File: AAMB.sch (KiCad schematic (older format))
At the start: 13 parts, among them J1 Screw_Terminal_01x04, J2 PJRAS4X2U01X, J3 SPKR, J4 SPKR, J5 Screw_Terminal_01x03, J6 Screw_Terminal_01x03, J7 Screw_Terminal_01x04

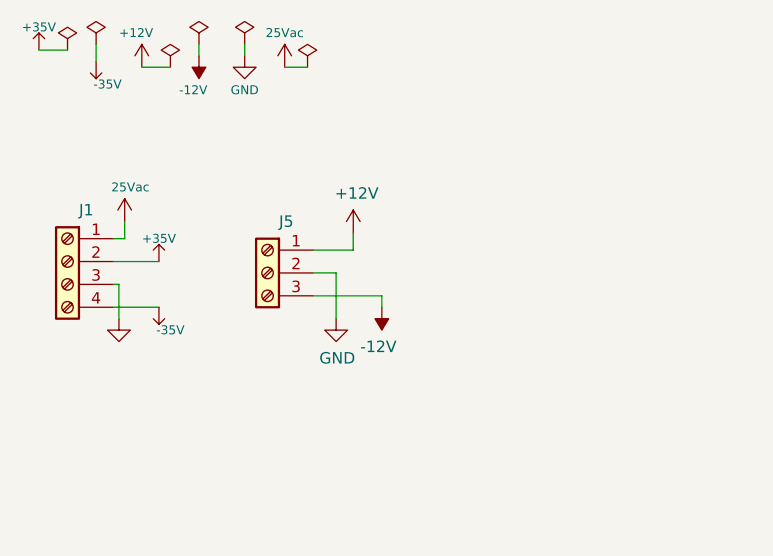
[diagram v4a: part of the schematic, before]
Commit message: Layout startover, sorting, some routing. Removed redundant fuses. BOM export.
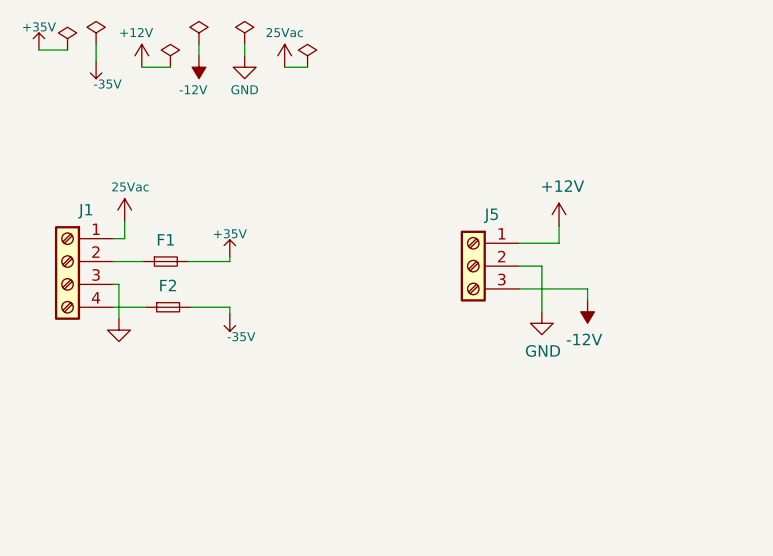
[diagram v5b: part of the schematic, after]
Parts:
- added F1, F2: Fuse_Small, Resistor_SMD:R_1206_3216Metric_Pad1.42x1.75mm_HandSolder, symbol Device:Fuse_Small
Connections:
- net +35V: now also F1.2; no longer J1.2 (Pin_2)
- net -35V: now also F2.2; no longer J1.4 (Pin_4)
- new net: F1.1, J1.2 (Pin_2)
- new net: F2.1, J1.4 (Pin_4)
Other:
- moved on the sheet: J5
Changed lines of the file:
@@
 L AAMB-rescue:+35V-Power-amp #PWR0106
 U 1 1 5E1EC4AA
-P 1100 1550
-F 0 "#PWR0106" H 1275 1375 50  0001 C CNN
-F 1 "+35V" H 1100 1650 39  0000 C CNN
-F 2 "" H 1100 1550 50  0001 C CNN
-F 3 "" H 1100 1550 50  0001 C CNN
-	1    1100 1550
+P 1410 1530
+F 0 "#PWR0106" H 1585 1355 50  0001 C CNN
+F 1 "+35V" H 1410 1630 39  0000 C CNN
+F 2 "" H 1410 1530 50  0001 C CNN
+F 3 "" H 1410 1530 50  0001 C CNN
+	1    1410 1530
 	1    0    0    -1
 $EndComp
@@
 L AAMB-rescue:-35V-Power-amp #PWR0107
 U 1 1 5E1EDDCB
-P 1100 1750
-F 0 "#PWR0107" H 1275 1575 50  0001 C CNN
-F 1 "-35V" H 1150 1650 39  0000 C CNN
-F 2 "" H 1100 1750 50  0001 C CNN
-F 3 "" H 1100 1750 50  0001 C CNN
-	1    1100 1750
-	1    0    0    -1
-$EndComp
-Wire Wire Line
-	900  1750 1100 1750
-Wire Wire Line
-	900  1550 1100 1550
+P 1410 1780
+F 0 "#PWR0107" H 1585 1605 50  0001 C CNN
+F 1 "-35V" H 1460 1680 39  0000 C CNN
+F 2 "" H 1410 1780 50  0001 C CNN
+F 3 "" H 1410 1780 50  0001 C CNN
+	1    1410 1780
+	1    0    0    -1
+$EndComp
 $Comp
 L power:PWR_FLAG #FLG0101
@@
 L Connector:Screw_Terminal_01x03 J5
 U 1 1 5E426C78
-P 1575 1600
-F 0 "J5" H 1493 1825 50  0000 C CNN
-F 1 "Screw_Terminal_01x03" H 1493 1826 50  0001 C CNN
-F 2 "TerminalBlock_Phoenix:TerminalBlock_Phoenix_MKDS-1,5-3_1x03_P5.00mm_Horizontal" H 1575 1600 50  0001 C CNN
-F 3 "https://media.digikey.com/pdf/Data%20Sheets/Phoenix%20Contact%20PDFs/1935174.pdf" H 1575 1600 50  0001 C CNN
-F 4 "https://www.digikey.com/product-detail/en/phoenix-contact/1935174/277-1578-ND/568615" H 1575 1600 50  0001 C CNN "DigiKey"
-F 5 "Phoenix Contact" H 1575 1600 50  0001 C CNN "MFG"
-F 6 "1935174" H 1575 1600 50  0001 C CNN "MPN"
-	1    1575 1600
+P 2475 1570
+F 0 "J5" H 2393 1795 50  0000 C CNN
+F 1 "Screw_Terminal_01x03" H 2393 1796 50  0001 C CNN
+F 2 "TerminalBlock_Phoenix:TerminalBlock_Phoenix_MKDS-1,5-3_1x03_P5.00mm_Horizontal" H 2475 1570 50  0001 C CNN
+F 3 "https://media.digikey.com/pdf/Data%20Sheets/Phoenix%20Contact%20PDFs/1935174.pdf" H 2475 1570 50  0001 C CNN
+F 4 "https://www.digikey.com/product-detail/en/phoenix-contact/1935174/277-1578-ND/568615" H 2475 1570 50  0001 C CNN "DigiKey"
+F 5 "Phoenix Contact" H 2475 1570 50  0001 C CNN "MFG"
+F 6 "1935174" H 2475 1570 50  0001 C CNN "MPN"
+	1    2475 1570
 	-1   0    0    -1
 $EndComp
@@
 L power:+12V #PWR09
 U 1 1 5E4290D4
-P 1950 1425
-F 0 "#PWR09" H 1950 1275 50  0001 C CNN
-F 1 "+12V" H 1965 1598 50  0000 C CNN
-F 2 "" H 1950 1425 50  0001 C CNN
-F 3 "" H 1950 1425 50  0001 C CNN
-	1    1950 1425
+P 2850 1395
+F 0 "#PWR09" H 2850 1245 50  0001 C CNN
+F 1 "+12V" H 2865 1568 50  0000 C CNN
+F 2 "" H 2850 1395 50  0001 C CNN
+F 3 "" H 2850 1395 50  0001 C CNN
+	1    2850 1395
 	1    0    0    -1
 $EndComp
@@
 L power:-12V #PWR010
 U 1 1 5E429F52
-P 2075 1750
-F 0 "#PWR010" H 2075 1850 50  0001 C CNN
-F 1 "-12V" H 2090 1923 50  0000 C CNN
-F 2 "" H 2075 1750 50  0001 C CNN
-F 3 "" H 2075 1750 50  0001 C CNN
-	1    2075 1750
+P 2975 1720
+F 0 "#PWR010" H 2975 1820 50  0001 C CNN
+F 1 "-12V" H 2990 1893 50  0000 C CNN
+F 2 "" H 2975 1720 50  0001 C CNN
+F 3 "" H 2975 1720 50  0001 C CNN
+	1    2975 1720
 	-1   0    0    1
 $EndComp
@@
 L power:GND #PWR08
 U 1 1 5E42A7CB
-P 1875 1800
-F 0 "#PWR08" H 1875 1550 50  0001 C CNN
-F 1 "GND" H 1880 1627 50  0000 C CNN
-F 2 "" H 1875 1800 50  0001 C CNN
-F 3 "" H 1875 1800 50  0001 C CNN
-	1    1875 1800
-	1    0    0    -1
-$EndComp
-Wire Wire Line
-	1875 1800 1875 1600
-Wire Wire Line
-	1875 1600 1775 1600
-Wire Wire Line
-	1950 1425 1950 1500
-Wire Wire Line
-	1950 1500 1775 1500
-Wire Wire Line
-	2075 1700 1775 1700
-Wire Wire Line
-	2075 1750 2075 1700
+P 2775 1770
+F 0 "#PWR08" H 2775 1520 50  0001 C CNN
+F 1 "GND" H 2780 1597 50  0000 C CNN
+F 2 "" H 2775 1770 50  0001 C CNN
+F 3 "" H 2775 1770 50  0001 C CNN
+	1    2775 1770
+	1    0    0    -1
+$EndComp
+Wire Wire Line
+	2775 1770 2775 1570
+Wire Wire Line
+	2775 1570 2675 1570
+Wire Wire Line
+	2850 1395 2850 1470
+Wire Wire Line
+	2850 1470 2675 1470
+Wire Wire Line
+	2975 1670 2675 1670
+Wire Wire Line
+	2975 1720 2975 1670
 Text Label 6725 4175 2    50   ~ 0
 line_audio_R
@@
 F 1 "TP" H 4950 5129 50  0000 C CNN
 F 2 "TestPoint:TestPoint_2Pads_Pitch2.54mm_Drill0.8mm" H 4950 5025 50  0001 C CNN
-F 3 "~" H 4950 5025 50  0001 C CNN
+F 3 "" H 4950 5025 50  0001 C CNN
 	1    4950 5025
 	1    0    0    -1
@@
 F 1 "TP" H 4950 5554 50  0001 C CNN
 F 2 "TestPoint:TestPoint_2Pads_Pitch2.54mm_Drill0.8mm" H 4950 5450 50  0001 C CNN
-F 3 "~" H 4950 5450 50  0001 C CNN
+F 3 "" H 4950 5450 50  0001 C CNN
 F 4 "pre_vol_audio_R" H 4945 5365 50  0000 C CNN "Note"
 	1    4950 5450
@@
 F 1 "TP" H 6700 4729 50  0000 C CNN
 F 2 "TestPoint:TestPoint_2Pads_Pitch2.54mm_Drill0.8mm" H 6700 4625 50  0001 C CNN
-F 3 "~" H 6700 4625 50  0001 C CNN
+F 3 "" H 6700 4625 50  0001 C CNN
 	1    6700 4625
 	1    0    0    -1
@@
 F 1 "TP" H 6700 5154 50  0000 C CNN
 F 2 "TestPoint:TestPoint_2Pads_Pitch2.54mm_Drill0.8mm" H 6700 5050 50  0001 C CNN
-F 3 "~" H 6700 5050 50  0001 C CNN
+F 3 "" H 6700 5050 50  0001 C CNN
 	1    6700 5050
 	1    0    0    -1
@@
 F 1 "TP" H 8350 4829 50  0000 C CNN
 F 2 "TestPoint:TestPoint_2Pads_Pitch2.54mm_Drill0.8mm" H 8350 4725 50  0001 C CNN
-F 3 "~" H 8350 4725 50  0001 C CNN
+F 3 "" H 8350 4725 50  0001 C CNN
 	1    8350 4725
 	1    0    0    -1
@@
 F 1 "TP" H 8350 5254 50  0000 C CNN
 F 2 "TestPoint:TestPoint_2Pads_Pitch2.54mm_Drill0.8mm" H 8350 5150 50  0001 C CNN
-F 3 "~" H 8350 5150 50  0001 C CNN
+F 3 "" H 8350 5150 50  0001 C CNN
 	1    8350 5150
 	1    0    0    -1
@@
 	1    0    0    -1
 $EndComp
+$Comp
+L Device:Fuse_Small F?
+U 1 1 5E9A4ADA
+P 1130 1550
+AR Path="/5C7F608F/5E9A4ADA" Ref="F?"  Part="1"
+AR Path="/5E9A4ADA" Ref="F1"  Part="1"
+F 0 "F1" H 1130 1643 50  0000 C CNN
+F 1 "Fuse_Small" H 1130 1644 50  0001 C CNN
+F 2 "Resistor_SMD:R_1206_3216Metric_Pad1.42x1.75mm_HandSolder" H 1130 1550 50  0001 C CNN
+F 3 "https://belfuse.com/resources/datasheets/circuitprotection/ds-cp-c1f-series.pdf" H 1130 1550 50  0001 C CNN
+F 4 "https://www.digikey.com/product-detail/en/bel-fuse-inc/C1F-3/507-1883-1-ND/4968162" H 1130 1550 50  0001 C CNN "DigiKey"
+F 5 "Bel Fuse Inc." H 1130 1550 50  0001 C CNN "MFG"
+F 6 "C1F 3" H 1130 1550 50  0001 C CNN "MPN"
+	1    1130 1550
+	1    0    0    -1
+$EndComp
+Wire Wire Line
+	900  1550 1030 1550
+Wire Wire Line
+	1230 1550 1410 1550
+Wire Wire Line
+	1410 1550 1410 1530
+$Comp
+L Device:Fuse_Small F?
+U 1 1 5E9B7B14
+P 1140 1750
+AR Path="/5C7F608F/5E9B7B14" Ref="F?"  Part="1"
+AR Path="/5E9B7B14" Ref="F2"  Part="1"
+F 0 "F2" H 1140 1843 50  0000 C CNN
+F 1 "Fuse_Small" H 1140 1844 50  0001 C CNN
+F 2 "Resistor_SMD:R_1206_3216Metric_Pad1.42x1.75mm_HandSolder" H 1140 1750 50  0001 C CNN
+F 3 "https://belfuse.com/resources/datasheets/circuitprotection/ds-cp-c1f-series.pdf" H 1140 1750 50  0001 C CNN
+F 4 "https://www.digikey.com/product-detail/en/bel-fuse-inc/C1F-3/507-1883-1-ND/4968162" H 1140 1750 50  0001 C CNN "DigiKey"
+F 5 "Bel Fuse Inc." H 1140 1750 50  0001 C CNN "MFG"
+F 6 "C1F 3" H 1140 1750 50  0001 C CNN "MPN"
+	1    1140 1750
+	1    0    0    -1
+$EndComp
+Wire Wire Line
+	900  1750 1040 1750
+Wire Wire Line
+	1240 1750 1410 1750
+Wire Wire Line
+	1410 1750 1410 1780
 $EndSCHEMATC

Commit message: Capturing layout progress.
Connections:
- net +35V_UNFUSED: now reaches F1.1, J1.2 (Pin_2)
- net -35V_UNFUSED: now reaches F2.1, J1.4 (Pin_4)
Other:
- moved on the sheet: F1, F2
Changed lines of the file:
@@
 $EndSheet
 Wire Wire Line
-	900  1650 925  1650
+	890  1650 925  1650
 Wire Wire Line
 	925  1800 925  1650
@@
 L AAMB-rescue:+35V-Power-amp #PWR0106
 U 1 1 5E1EC4AA
-P 1410 1530
-F 0 "#PWR0106" H 1585 1355 50  0001 C CNN
-F 1 "+35V" H 1410 1630 39  0000 C CNN
-F 2 "" H 1410 1530 50  0001 C CNN
-F 3 "" H 1410 1530 50  0001 C CNN
-	1    1410 1530
+P 1985 1530
+F 0 "#PWR0106" H 2160 1355 50  0001 C CNN
+F 1 "+35V" H 1985 1630 39  0000 C CNN
+F 2 "" H 1985 1530 50  0001 C CNN
+F 3 "" H 1985 1530 50  0001 C CNN
+	1    1985 1530
 	1    0    0    -1
 $EndComp
@@
 L AAMB-rescue:-35V-Power-amp #PWR0107
 U 1 1 5E1EDDCB
-P 1410 1780
-F 0 "#PWR0107" H 1585 1605 50  0001 C CNN
-F 1 "-35V" H 1460 1680 39  0000 C CNN
-F 2 "" H 1410 1780 50  0001 C CNN
-F 3 "" H 1410 1780 50  0001 C CNN
-	1    1410 1780
+P 1985 1780
+F 0 "#PWR0107" H 2160 1605 50  0001 C CNN
+F 1 "-35V" H 2035 1680 39  0000 C CNN
+F 2 "" H 1985 1780 50  0001 C CNN
+F 3 "" H 1985 1780 50  0001 C CNN
+	1    1985 1780
 	1    0    0    -1
 $EndComp
@@
 L Connector:Screw_Terminal_01x04 J1
 U 1 1 5E402B60
-P 700 1550
-F 0 "J1" H 618 1775 50  0000 C CNN
-F 1 "Screw_Terminal_01x04" H 618 1776 50  0001 C CNN
-F 2 "TerminalBlock_Phoenix:TerminalBlock_Phoenix_MKDS-1,5-4_1x04_P5.00mm_Horizontal" H 700 1550 50  0001 C CNN
-F 3 "https://www.cuidevices.com/product/resource/tb001-500.pdf" H 700 1550 50  0001 C CNN
-F 4 "https://www.digikey.com/product-detail/en/cui-devices/TB001-500-04BE/102-6136-ND/10064060" H 700 1550 50  0001 C CNN "DigiKey"
-F 5 "CUI Devices" H 700 1550 50  0001 C CNN "MFG"
-F 6 "TB001-500-04BE" H 700 1550 50  0001 C CNN "MPN"
-	1    700  1550
+P 690 1550
+F 0 "J1" H 608 1775 50  0000 C CNN
+F 1 "Screw_Terminal_01x04" H 608 1776 50  0001 C CNN
+F 2 "TerminalBlock_Phoenix:TerminalBlock_Phoenix_MKDS-1,5-4_1x04_P5.00mm_Horizontal" H 690 1550 50  0001 C CNN
+F 3 "https://www.cuidevices.com/product/resource/tb001-500.pdf" H 690 1550 50  0001 C CNN
+F 4 "https://www.digikey.com/product-detail/en/cui-devices/TB001-500-04BE/102-6136-ND/10064060" H 690 1550 50  0001 C CNN "DigiKey"
+F 5 "CUI Devices" H 690 1550 50  0001 C CNN "MFG"
+F 6 "TB001-500-04BE" H 690 1550 50  0001 C CNN "MPN"
+	1    690  1550
 	-1   0    0    -1
 $EndComp
@@
 	1750 700  1650 700
 Wire Wire Line
-	900  1450 950  1450
+	890  1450 950  1450
 $Comp
 L AAMB-rescue:25Vac-power #PWR0124
@@
 L Device:Fuse_Small F?
 U 1 1 5E9A4ADA
-P 1130 1550
+P 1695 1550
 AR Path="/5C7F608F/5E9A4ADA" Ref="F?"  Part="1"
 AR Path="/5E9A4ADA" Ref="F1"  Part="1"
-F 0 "F1" H 1130 1643 50  0000 C CNN
-F 1 "Fuse_Small" H 1130 1644 50  0001 C CNN
-F 2 "Resistor_SMD:R_1206_3216Metric_Pad1.42x1.75mm_HandSolder" H 1130 1550 50  0001 C CNN
-F 3 "https://belfuse.com/resources/datasheets/circuitprotection/ds-cp-c1f-series.pdf" H 1130 1550 50  0001 C CNN
-F 4 "https://www.digikey.com/product-detail/en/bel-fuse-inc/C1F-3/507-1883-1-ND/4968162" H 1130 1550 50  0001 C CNN "DigiKey"
-F 5 "Bel Fuse Inc." H 1130 1550 50  0001 C CNN "MFG"
-F 6 "C1F 3" H 1130 1550 50  0001 C CNN "MPN"
-	1    1130 1550
-	1    0    0    -1
-$EndComp
-Wire Wire Line
-	900  1550 1030 1550
-Wire Wire Line
-	1230 1550 1410 1550
-Wire Wire Line
-	1410 1550 1410 1530
+F 0 "F1" H 1695 1643 50  0000 C CNN
+F 1 "Fuse_Small" H 1695 1644 50  0001 C CNN
+F 2 "Resistor_SMD:R_1206_3216Metric_Pad1.42x1.75mm_HandSolder" H 1695 1550 50  0001 C CNN
+F 3 "https://belfuse.com/resources/datasheets/circuitprotection/ds-cp-c1f-series.pdf" H 1695 1550 50  0001 C CNN
+F 4 "https://www.digikey.com/product-detail/en/bel-fuse-inc/C1F-3/507-1883-1-ND/4968162" H 1695 1550 50  0001 C CNN "DigiKey"
+F 5 "Bel Fuse Inc." H 1695 1550 50  0001 C CNN "MFG"
+F 6 "C1F 3" H 1695 1550 50  0001 C CNN "MPN"
+	1    1695 1550
+	1    0    0    -1
+$EndComp
+Wire Wire Line
+	1795 1550 1985 1550
+Wire Wire Line
+	1985 1550 1985 1530
 $Comp
 L Device:Fuse_Small F?
 U 1 1 5E9B7B14
-P 1140 1750
+P 1715 1750
 AR Path="/5C7F608F/5E9B7B14" Ref="F?"  Part="1"
 AR Path="/5E9B7B14" Ref="F2"  Part="1"
-F 0 "F2" H 1140 1843 50  0000 C CNN
-F 1 "Fuse_Small" H 1140 1844 50  0001 C CNN
-F 2 "Resistor_SMD:R_1206_3216Metric_Pad1.42x1.75mm_HandSolder" H 1140 1750 50  0001 C CNN
-F 3 "https://belfuse.com/resources/datasheets/circuitprotection/ds-cp-c1f-series.pdf" H 1140 1750 50  0001 C CNN
-F 4 "https://www.digikey.com/product-detail/en/bel-fuse-inc/C1F-3/507-1883-1-ND/4968162" H 1140 1750 50  0001 C CNN "DigiKey"
-F 5 "Bel Fuse Inc." H 1140 1750 50  0001 C CNN "MFG"
-F 6 "C1F 3" H 1140 1750 50  0001 C CNN "MPN"
-	1    1140 1750
-	1    0    0    -1
-$EndComp
-Wire Wire Line
-	900  1750 1040 1750
-Wire Wire Line
-	1240 1750 1410 1750
-Wire Wire Line
-	1410 1750 1410 1780
+F 0 "F2" H 1715 1843 50  0000 C CNN
+F 1 "Fuse_Small" H 1715 1844 50  0001 C CNN
+F 2 "Resistor_SMD:R_1206_3216Metric_Pad1.42x1.75mm_HandSolder" H 1715 1750 50  0001 C CNN
+F 3 "https://belfuse.com/resources/datasheets/circuitprotection/ds-cp-c1f-series.pdf" H 1715 1750 50  0001 C CNN
+F 4 "https://www.digikey.com/product-detail/en/bel-fuse-inc/C1F-3/507-1883-1-ND/4968162" H 1715 1750 50  0001 C CNN "DigiKey"
+F 5 "Bel Fuse Inc." H 1715 1750 50  0001 C CNN "MFG"
+F 6 "C1F 3" H 1715 1750 50  0001 C CNN "MPN"
+	1    1715 1750
+	1    0    0    -1
+$EndComp
+Wire Wire Line
+	1815 1750 1985 1750
+Wire Wire Line
+	1985 1750 1985 1780
+Wire Wire Line
+	890  1550 1595 1550
+Wire Wire Line
+	890  1750 1615 1750
+Text Label 960  1550 0    50   ~ 0
++35V_UNFUSED
+Text Label 960  1750 0    50   ~ 0
+-35V_UNFUSED
 $EndSCHEMATC

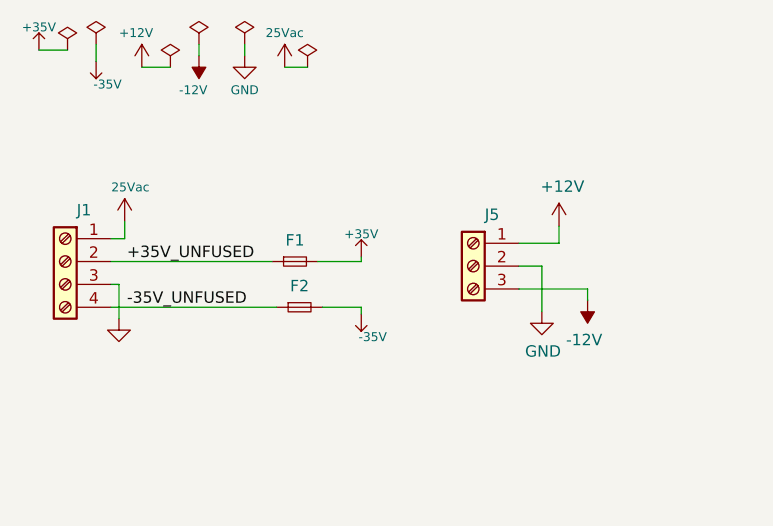
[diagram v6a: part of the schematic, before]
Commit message: Place and route complete. Silkscreen cleanup needed.
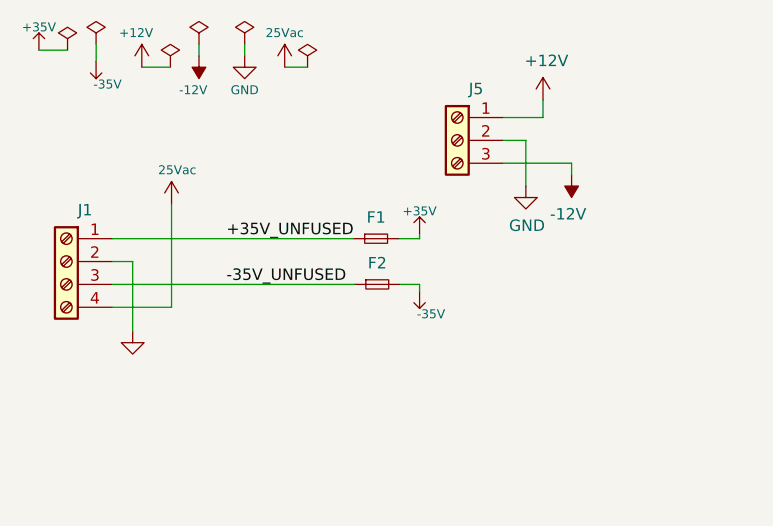
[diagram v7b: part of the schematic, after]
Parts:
- J3: DigiKey https://media.digikey.com/pdf/Data%20Sheets/Phoenix%20Conta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 -> https://www.digikey.com/products/en?keywords=1935161
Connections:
- net +35V_UNFUSED: now also J1.1 (Pin_1); no longer J1.2 (Pin_2)
- net -35V_UNFUSED: now also J1.3 (Pin_3); no longer J1.4 (Pin_4)
- net 25Vac: now also J1.4 (Pin_4); no longer J1.1 (Pin_1)
- net GND: now also J1.2 (Pin_2); no longer J1.3 (Pin_3)
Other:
- moved on the sheet: F1, F2, J5

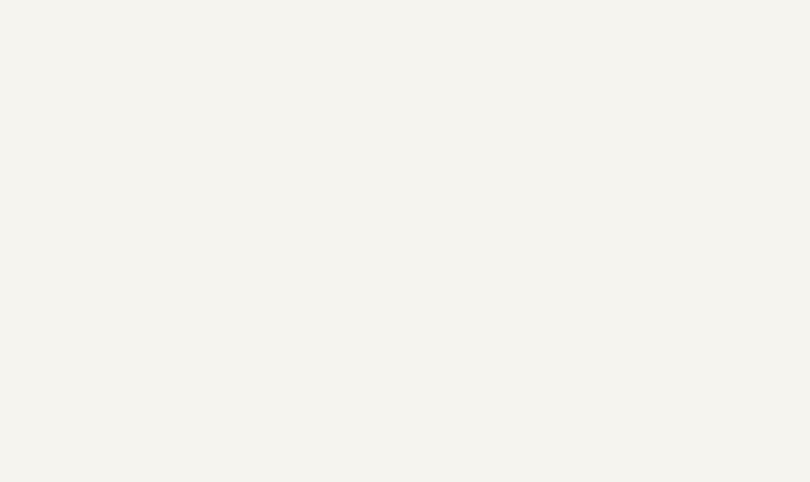
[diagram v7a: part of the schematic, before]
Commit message: Layout complete. Screw holes added and connected to GND.
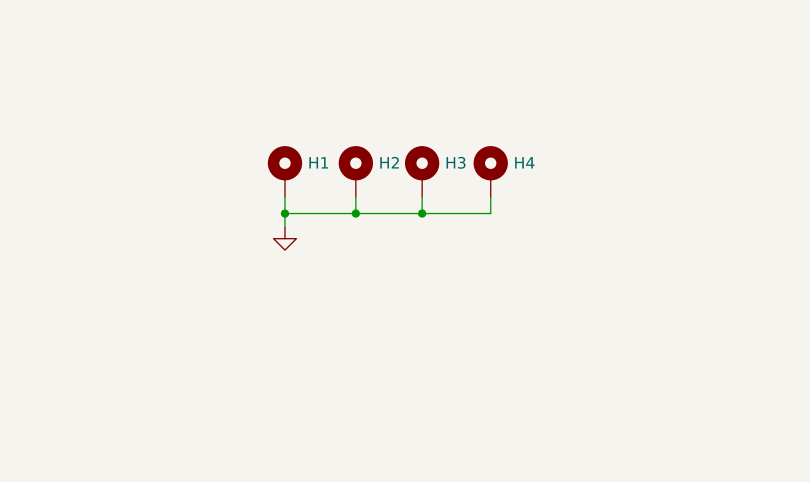
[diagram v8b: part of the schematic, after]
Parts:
- added H1, H2, H3, H4: MountingHole_Pad, MountingHole:MountingHole_3.2mm_M3_Pad, symbol Mechanical:MountingHole_Pad
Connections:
- net GND: now also H1.1, H2.1, H3.1, H4.1
